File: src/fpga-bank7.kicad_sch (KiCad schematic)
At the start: 1 part

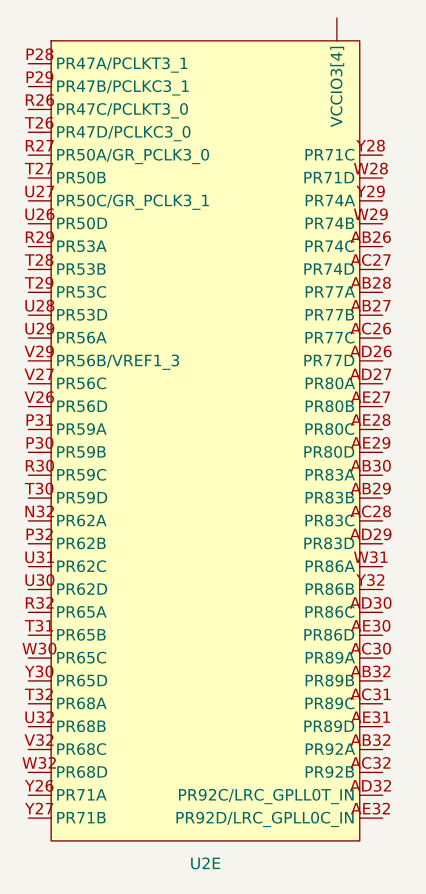
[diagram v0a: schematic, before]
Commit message: Finishes FPGA symbol
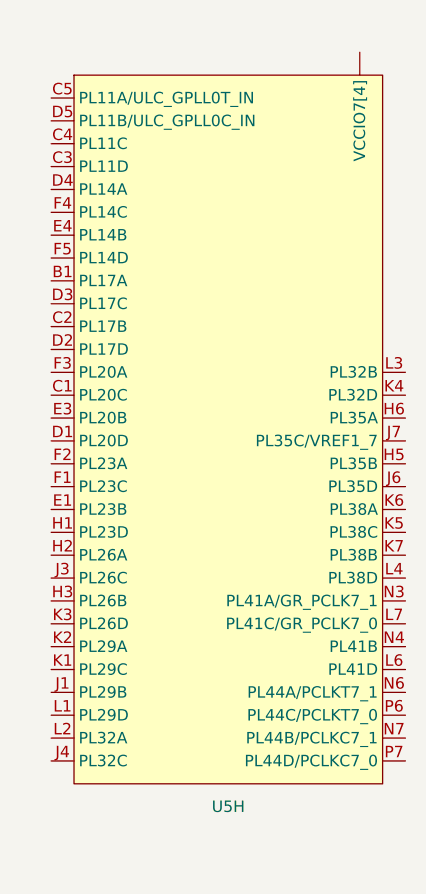
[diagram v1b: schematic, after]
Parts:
- removed U2: ~, symbol ECAP5-BSOM:LFE5U-85F-*BG756*
- added U5: ~, symbol ECAP5-BSOM:LFE5U-85F-*BG756*
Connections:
- new net VCCIO7: U5. (VCCIO7[4]), U5.M10 (VCCIO7), U5.P10 (VCCIO7), U5.R10 (VCCIO7), U5.T10 (VCCIO7)
